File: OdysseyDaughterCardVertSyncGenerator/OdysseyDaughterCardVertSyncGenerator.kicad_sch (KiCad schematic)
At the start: 13 parts

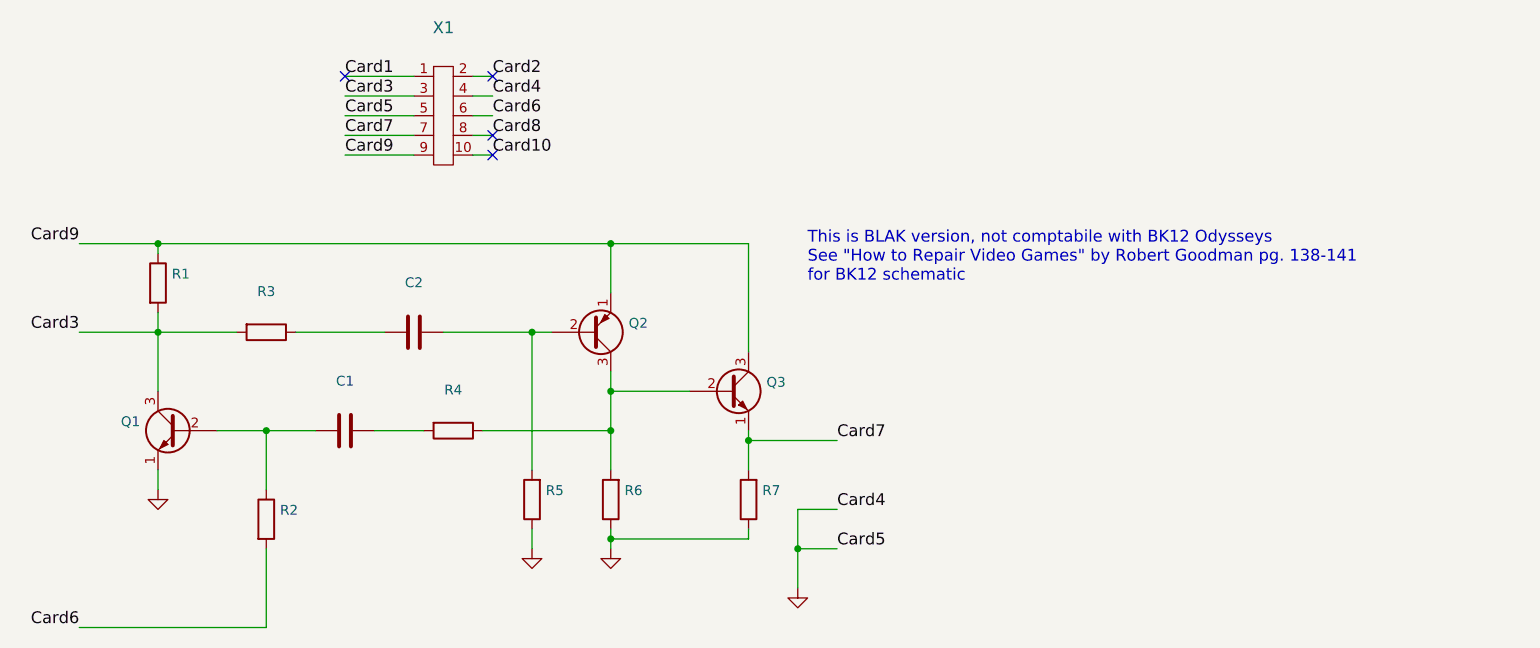
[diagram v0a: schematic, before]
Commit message: OdysseyDaughterCardVertSyncGenerator wider transistor footprint, add logo, generate pdf, images, 3d models
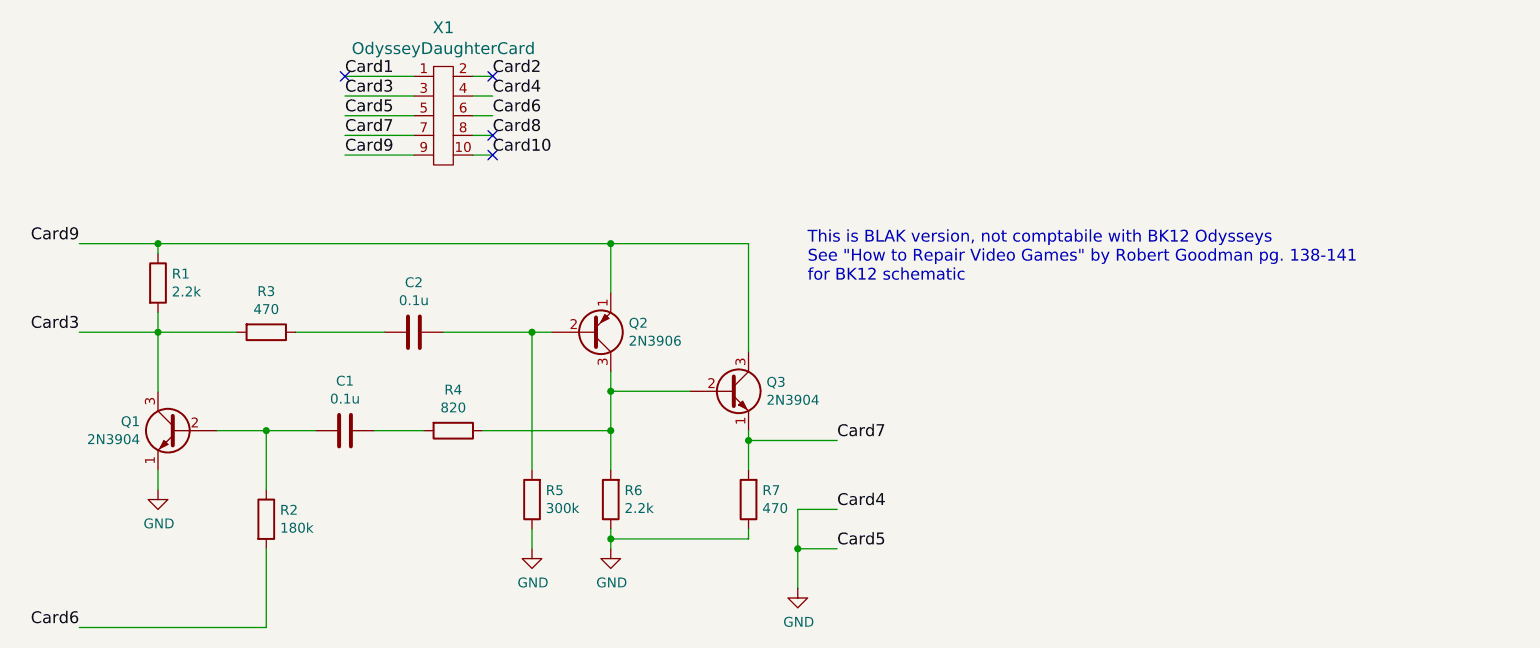
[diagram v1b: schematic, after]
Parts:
- C1, C2: value (none) -> 0.1u; footprint (none) -> Capacitor_THT:C_Disc_D5.1mm_W3.2mm_P5.00mm
- Q1, Q3: value (none) -> 2N3904; footprint (none) -> Package_TO_SOT_THT:TO-92_Inline_Wide
- Q2: value (none) -> 2N3906; footprint (none) -> Package_TO_SOT_THT:TO-92_Inline_Wide
- R1, R6: value (none) -> 2.2k; footprint (none) -> Resistor_THT:R_Axial_DIN0207_L6.3mm_D2.5mm_P7.62mm_Horizontal
- R2: value (none) -> 180k; footprint (none) -> Resistor_THT:R_Axial_DIN0207_L6.3mm_D2.5mm_P7.62mm_Horizontal
- R3, R7: value (none) -> 470; footprint (none) -> Resistor_THT:R_Axial_DIN0207_L6.3mm_D2.5mm_P7.62mm_Horizontal
- R4: value (none) -> 820; footprint (none) -> Resistor_THT:R_Axial_DIN0207_L6.3mm_D2.5mm_P7.62mm_Horizontal
- R5: value (none) -> 300k; footprint (none) -> Resistor_THT:R_Axial_DIN0207_L6.3mm_D2.5mm_P7.62mm_Horizontal
- X1: value (none) -> OdysseyDaughterCard; footprint (none) -> Odyssey_Daughter_Card:Odyssey_Daughter_Card
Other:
- company: University of Pittsburgh - Odyssey Restoration Project -> University of Pittsburgh - OdysseyNow
